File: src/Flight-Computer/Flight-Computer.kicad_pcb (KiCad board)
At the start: 4 copper layers, 113.5 x 45.7 mm, 109 parts, among them J1 Jumper_NO, P1 282837-2, P10 Micro_SD_Card, P2 647676-2, P3 USB, P4 282837-6, P5 440054-3, P6 440054-3, P7 440054-3, P8 3220-20-0200-00, P9 440054-3, Q1 QS5U17TR, Q2 QS5U17TR, Q3 QS5U17TR, Q4 QS5U17TR, Q5 QS5U17TR, Q6 QS5U17TR, U1 STM32H750VBTx, U10 RFM95W-868S2, U11 BMP390, U2 LMS8117AMP-3.3_NOPB, U3 CP2102-GMR(QFN28), U4 SST25VF040B-50-4I-S2AE-T, U5 TS391IYLT, U6 TS391IYLT, U7 TS391IYLT, U8 MPU-9250, U9 MAX-8C-0-10, Y1 ECS-240-18-33-JGN-TR

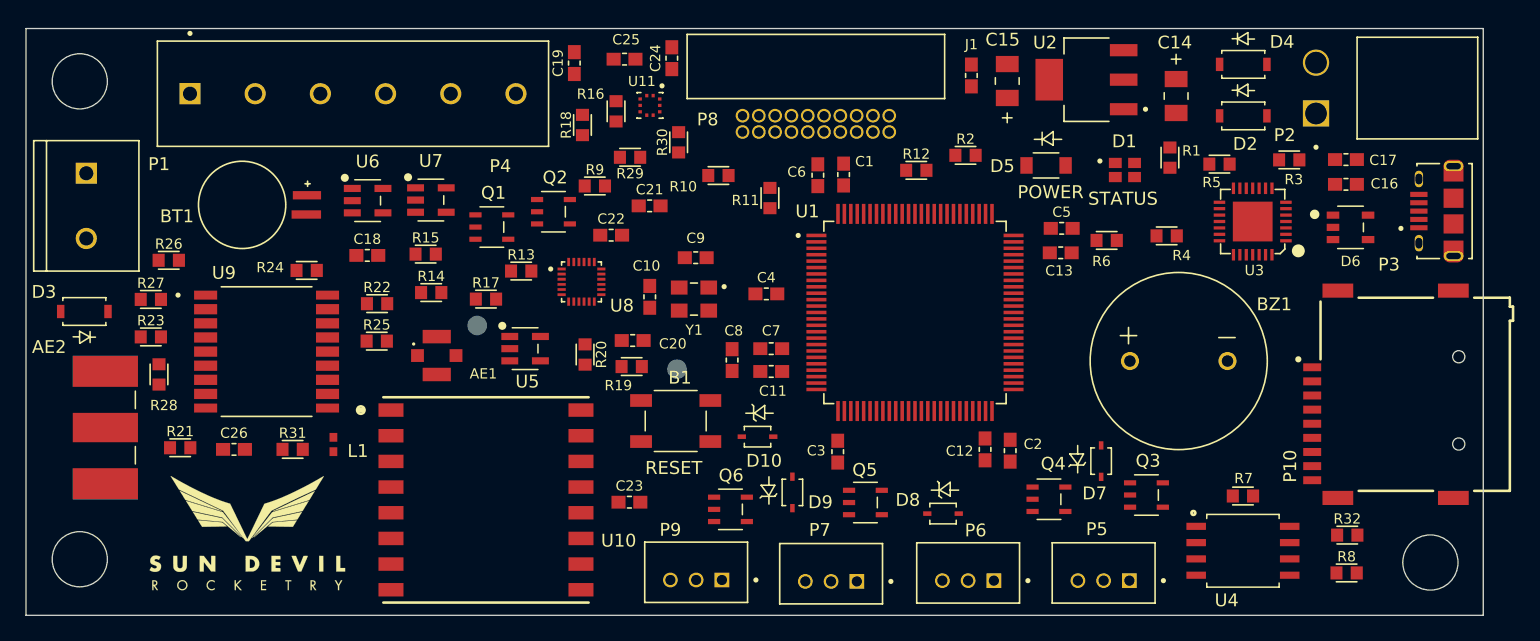
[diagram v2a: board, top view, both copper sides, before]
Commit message: routed main peripheral functionality excluding parachute deployment circuitry
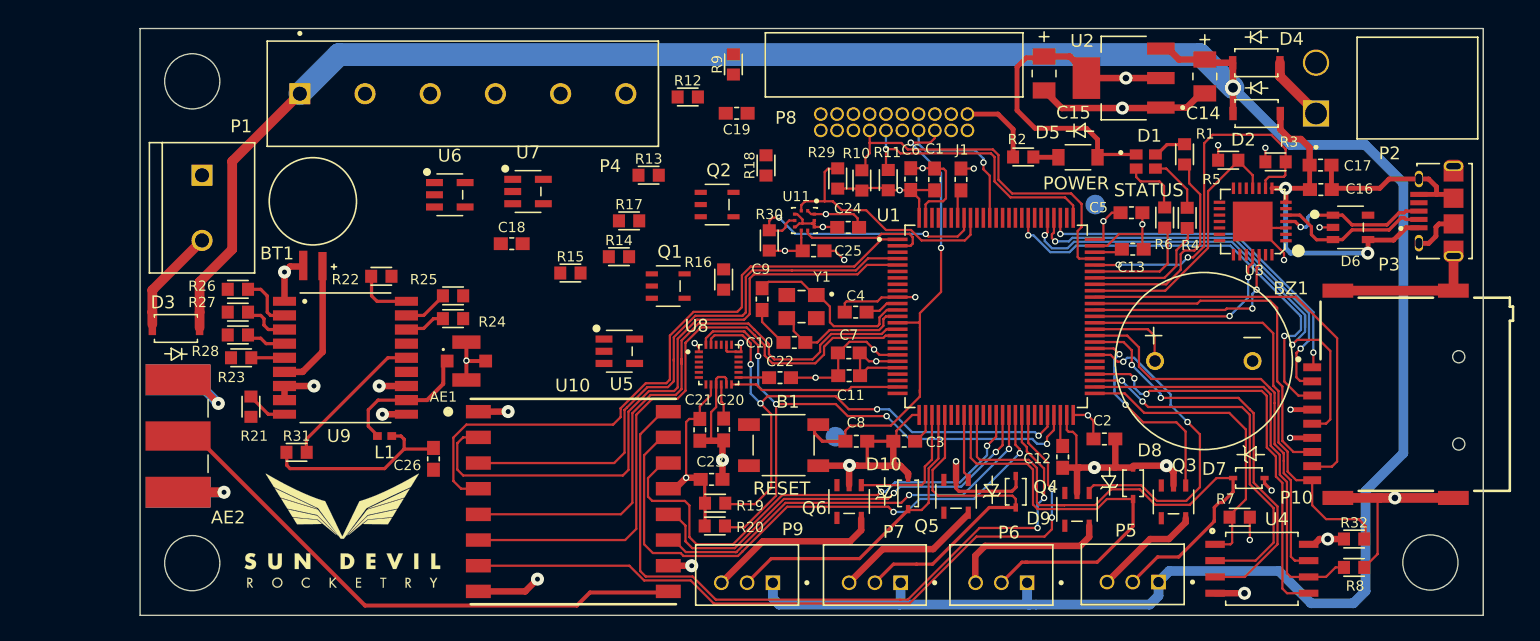
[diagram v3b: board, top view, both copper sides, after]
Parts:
- AE2: value CONN_142-0701-851_CIN -> 142-0701-851
- moved TP2 49.1 mm to (156.5, 69.6)
- moved C25 21.0 mm to (134.5, 73.2)
- moved C24 19.0 mm to (137.2, 71.4), turned to 180 degrees
- moved R12 18.7 mm to (124.7, 61.2)
- moved C21 17.9 mm to (125.7, 87.1), turned to -90 degrees
- moved D9 17.4 mm to (150.3, 92.0)
- moved C22 17.2 mm to (131.9, 83.1)
- moved R20 16.8 mm to (126.8, 94.6), turned to 180 degrees
- moved R29 16.3 mm to (136.4, 67.6), turned to -90 degrees
- moved C26 15.6 mm to (104.9, 89.4), turned to -90 degrees
- moved R16 15.6 mm to (127.5, 75.4)
- moved U11 15.0 mm to (133.9, 70.9)
- moved D8 15.0 mm to (159.4, 91.3), turned to 90 degrees
- moved R14 14.9 mm to (119.4, 73.7)
- moved R18 14.6 mm to (130.8, 66.5)
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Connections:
- U1 pad 17: W_IO0 -> unconnected-(U1-Pad17)
- U1 pad 18: W_IO1 -> unconnected-(U1-Pad18)
- U1 pad 2: unconnected-(U1-Pad2) -> BP_INT
- U1 pad 24: MOTOR1_PWM -> IMU_INT
- U1 pad 25: MOTOR2_PWM -> unconnected-(U1-Pad25)
- U1 pad 28: MOTOR1_EN -> MOTOR4_EN
- U1 pad 29: MOTOR3_PWM -> MOTOR4_PWM
- U1 pad 30: MOTOR4_PWM -> MOTOR2_PWM
- U1 pad 31: BEEP -> unconnected-(U1-Pad31)
- U1 pad 32: W_IO2 -> unconnected-(U1-Pad32)
- U1 pad 33: W_IO3 -> MOTOR2_EN
- U1 pad 34: unconnected-(U1-Pad34) -> MOTOR3_PWM
- U1 pad 35: unconnected-(U1-Pad35) -> MOTOR1_PWM
- U1 pad 38: unconnected-(U1-Pad38) -> W_IO0
- U1 pad 39: unconnected-(U1-Pad39) -> W_IO4
- U1 pad 40: STATUS_R -> W_IO3
- U1 pad 41: STATUS_G -> W_IO1
- U1 pad 42: STATUS_B -> W_IO2
- U1 pad 43: unconnected-(U1-Pad43) -> W_IO5
- U1 pad 46: BP_SCL -> SCL
- U1 pad 47: BP_SDA -> SDA
- U1 pad 57: ~{USB_RST} -> MOTOR3_EN
- U1 pad 58: ~{USB_SUSPEND} -> MOTOR1_EN
- U1 pad 61: BP_INT -> BEEP
- U1 pad 62: unconnected-(U1-Pad62) -> ~{SD_DETECT}
- U1 pad 63: W_IO4 -> RX_USB
- U1 pad 64: W_IO5 -> TX_USB
- U1 pad 67: MOTOR3_EN -> ~{USB_SUSPEND}
- U1 pad 68: RX_USB -> STATUS_B
- U1 pad 69: TX_USB -> STATUS_G
- U1 pad 70: MOTOR2_EN -> STATUS_R
- U1 pad 71: MOTOR4_EN -> ~{USB_RST}
- U1 pad 84: IMU_INT -> unconnected-(U1-Pad84)
- U1 pad 92: SCL -> BP_SCL
- U1 pad 93: SDA -> BP_SDA
- U1 pad 96: ~{SD_DETECT} -> unconnected-(U1-Pad96)
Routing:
- net Earth: track 0.00 -> 210.9 mm, vias 0 -> 30
- net VIN: track 0.00 -> 208.6 mm, vias 0 -> 1
- net 3.3V: track 0.00 -> 90.4 mm, vias 0 -> 15
- net W_IO5: track 0.00 -> 58.0 mm, vias 0 -> 2
- net W_IO2: track 0.00 -> 57.5 mm, vias 0 -> 2
- net W_MOSI: track 0.00 -> 51.4 mm
- net W_SCK: track 0.00 -> 50.4 mm
- net W_RST: track 0.00 -> 49.8 mm
- net W_SS: track 0.00 -> 48.2 mm
- net SDA: track 0.00 -> 47.4 mm, vias 0 -> 4
- net W_IO1: track 0.00 -> 45.8 mm, vias 0 -> 2
- net SCL: track 0.00 -> 45.1 mm, vias 0 -> 4
- net W_MISO: track 0.00 -> 44.6 mm
- net Net-(AE2-Pad1): track 0.00 -> 44.3 mm
- net MOTOR1_PWM: track 0.00 -> 41.2 mm
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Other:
- board size 113.5 x 45.7 mm -> 104.6 x 45.7 mm

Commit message: finished routing
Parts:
- removed TP1: TP, Flight-Computer:TP
- moved R18 20.1 mm to (112.5, 74.9), turned to 0 degrees
- moved R20 17.0 mm to (123.4, 78.0), turned to -90 degrees
- moved Q1 16.1 mm to (109.5, 67.6), turned to 180 degrees
- moved R19 15.9 mm to (126.5, 77.0)
- moved R12 13.8 mm to (112.8, 68.1), turned to -90 degrees
- moved R9 10.3 mm to (126.7, 68.8)
- moved U5 10.2 mm to (124.5, 72.2), turned to 180 degrees
- moved U6 10.0 mm to (115.6, 72.4), turned to 180 degrees
- moved AE1 9.91 mm to (117.4, 82.2)
- moved R14 9.70 mm to (128.8, 71.4), turned to 90 degrees
- moved R31 9.20 mm to (103.4, 89.9), turned to 180 degrees
- moved C23 8.99 mm to (132.6, 84.3), turned to 90 degrees
- moved R26 8.95 mm to (98.6, 77.2)
- moved R23 8.77 mm to (98.6, 83.1)
- moved U9 8.73 mm to (106.7, 82.8)
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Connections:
- U1 pad 25: unconnected-(U1-Pad25) -> GPS_INT
- U1 pad 3: unconnected-(U1-Pad3) -> ~{MAIN_CONT}
- U1 pad 31: unconnected-(U1-Pad31) -> ~{GPS_RST}
- U1 pad 32: unconnected-(U1-Pad32) -> GPS_TIM
- U1 pad 40: W_IO3 -> W_IO1
- U1 pad 41: W_IO1 -> W_IO3
- U1 pad 55: ~{MAIN_CONT} -> unconnected-(U1-Pad55)
- U1 pad 56: ~{DROGUE_CONT} -> unconnected-(U1-Pad56)
- U1 pad 7: unconnected-(U1-Pad7) -> DROGUE
- U1 pad 77: ~{GPS_RST} -> unconnected-(U1-Pad77)
- U1 pad 8: unconnected-(U1-Pad8) -> ~{DROGUE_CONT}
- U1 pad 81: ~{GPS_SBOOT} -> unconnected-(U1-Pad81)
- U1 pad 82: GPS_INT -> unconnected-(U1-Pad82)
- U1 pad 85: GPS_TIM -> unconnected-(U1-Pad85)
- U1 pad 86: DROGUE -> unconnected-(U1-Pad86)
- U1 pad 87: ~{SWITCH} -> MAIN
- U1 pad 88: MAIN -> ~{SWITCH}
- U1 pad 9: unconnected-(U1-Pad9) -> ~{GPS_SBOOT}
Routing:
- net GPS_TIM: track 0.00 -> 68.1 mm, vias 0 -> 2
- net ~{GPS_RST}: track 0.00 -> 63.1 mm, vias 0 -> 2
- net GPS_INT: track 0.00 -> 59.5 mm, vias 0 -> 2
- net GPS_RX: track 0.00 -> 58.9 mm, vias 0 -> 2
- net GPS_TX: track 0.00 -> 54.4 mm, vias 0 -> 2
- net MAIN: track 0.00 -> 40.5 mm, vias 0 -> 2
- net VIN_SW: track 0.00 -> 40.2 mm
- net ~{DROGUE_CONT}: track 0.00 -> 34.7 mm, vias 0 -> 2
- net ~{GPS_SBOOT}: track 0.00 -> 33.5 mm, vias 0 -> 2
- net DROGUE: track 0.00 -> 32.9 mm, vias 0 -> 2
- net VIN: track 208.6 -> 240.0 mm, vias 1 -> 3
- net ~{SWITCH}: track 0.00 -> 27.7 mm, vias 0 -> 2
- net ~{MAIN_CONT}: track 0.00 -> 25.7 mm, vias 0 -> 2
- net 3.3V: track 90.4 -> 114.2 mm, vias 15 -> 20
- net VCOMP: track 0.00 -> 22.0 mm
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- added copper zone on In2.Cu, net 3.3V
- added copper zone on In1.Cu, net Earth
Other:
- board size 104.6 x 45.7 mm -> 96.8 x 45.7 mm
- board text added: "DROGUE"
- board text added: "MAIN"
- board text added: "SWITCH"

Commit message: finished resolving DRC errors
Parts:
- AE2: value 142-0701-851 -> CONN_142-0701-851_CIN
- D10, D7, D8, D9: value MM3Z3V3B -> SOD-323FL_477AB_ONS
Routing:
- net SD_CLK: track 38.6 -> 37.5 mm
- net 3.3V: track 114.2 -> 113.7 mm
- net Earth: track 231.5 -> 231.3 mm, vias 38 -> 39

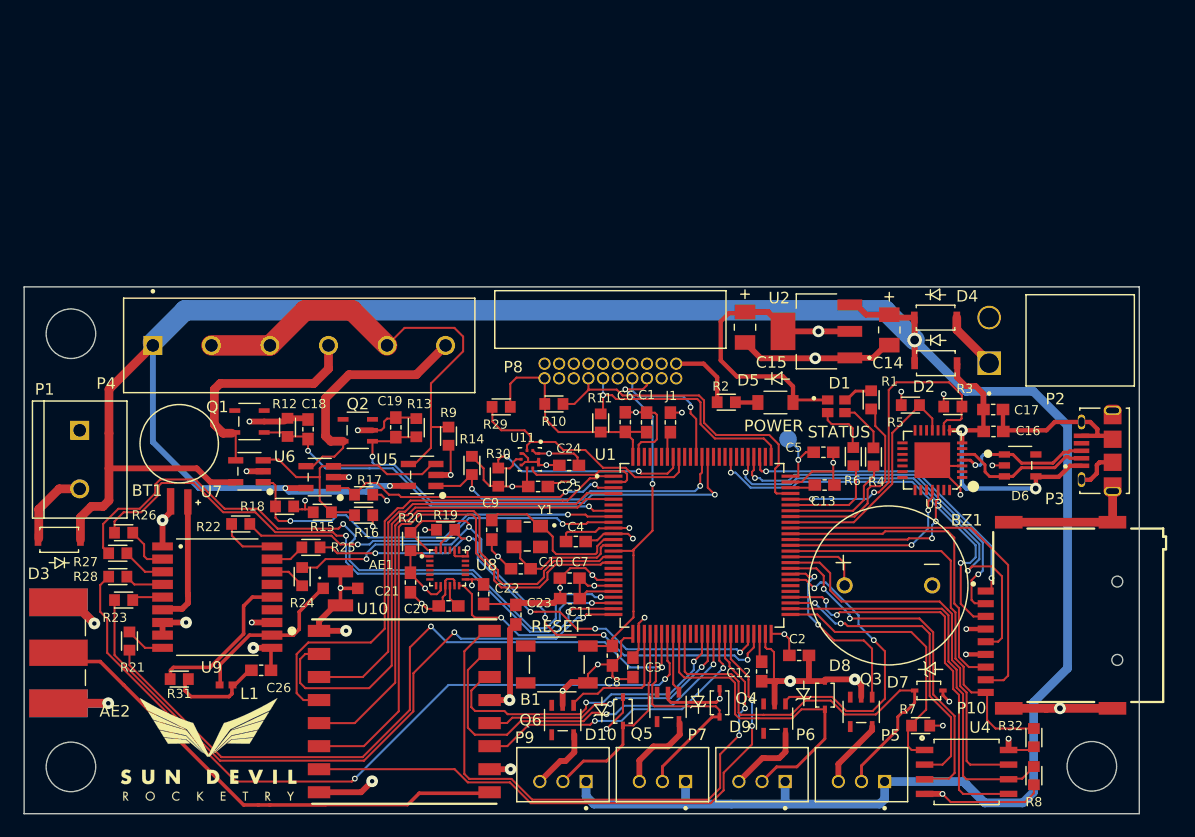
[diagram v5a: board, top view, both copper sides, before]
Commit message: started rev 2 routing
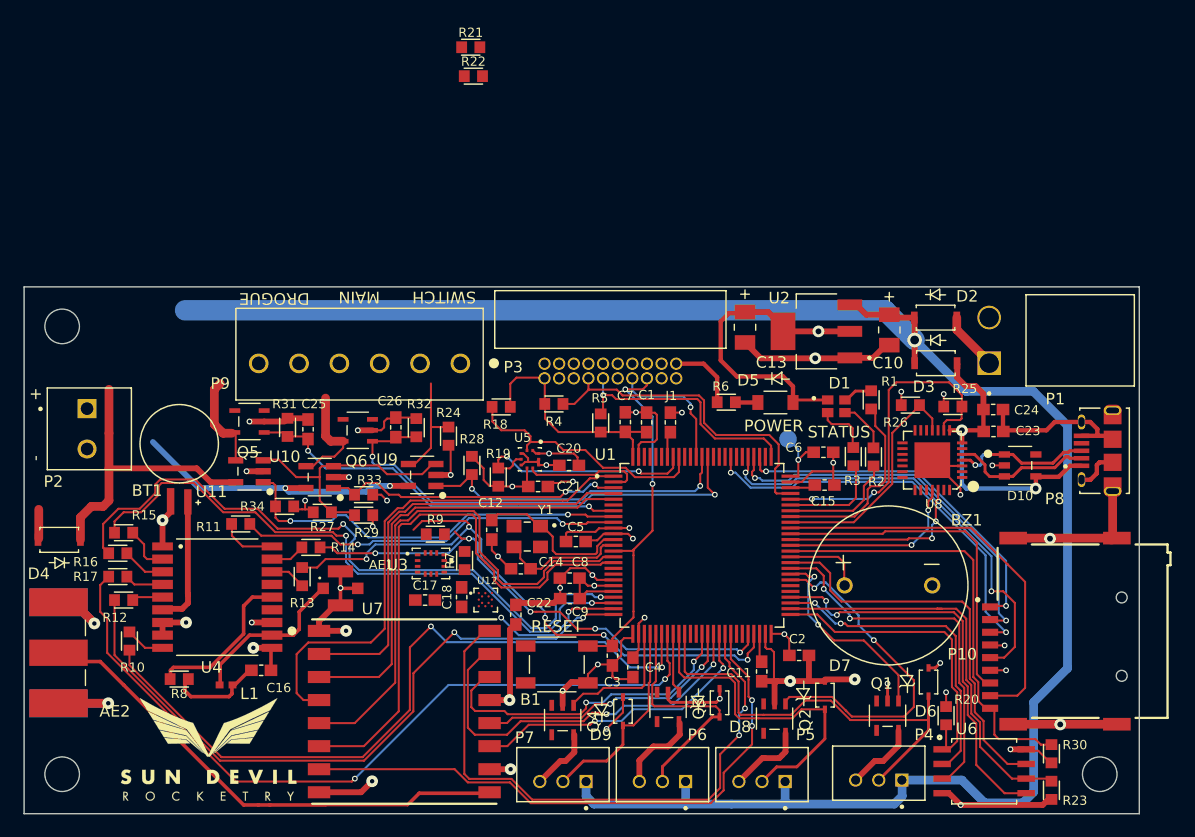
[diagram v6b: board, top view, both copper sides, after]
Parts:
- removed the C20 at (126.7, 83.6)
- removed the C21 at (123.4, 81.5)
- removed the C22 at (129.8, 82.5)
- removed the P1 at (94.7, 70.9)
- removed the P4 at (113.8, 61.0)
- removed the R19 at (126.5, 77.0)
- removed the R20 at (123.4, 78.0)
- removed the U8 at (126.7, 80.3)
- added C17: 0.1uF, Flight-Computer:CAP_0603, F.Cu at (124.7, 83.1)
- added C18: 0.1uF, Flight-Computer:CAP_0603, F.Cu at (127.9, 82.8)
- added P2: 1546551-2, Flight-Computer:1546551-2, F.Cu at (95.4, 68.2)
- added P9: 1984659, Flight-Computer:1984659, F.Cu at (127.8, 62.5)
- added R21: 10k, Flight-Computer:RES_0603, F.Cu at (128.7, 35.1)
- added R22: 20k, Flight-Computer:RES_0603, F.Cu at (128.9, 37.6)
- added R7: 10k, Engine-Controller:RES_0603, F.Cu at (128.1, 79.6)
- added R9: 10k, Engine-Controller:RES_0603, F.Cu at (125.6, 77.3)
- added U12: BMM150, Flight-Computer:BMM150, F.Cu at (130.0, 83.1)
- added U3: BMI323, Flight-Computer:BMI323, F.Cu at (125.2, 79.9)
- AE2: value CONN_142-0701-851_CIN -> 142-0701-851
- D6: renamed from D7; value SOD-323FL_477AB_ONS -> MM3Z3V3B
- D7: renamed from D8; value SOD-323FL_477AB_ONS -> MM3Z3V3B
- D8: renamed from D9; value SOD-323FL_477AB_ONS -> MM3Z3V3B
- D9: renamed from D10; value SOD-323FL_477AB_ONS -> MM3Z3V3B
- H1: footprint Flight-Computer:MountingHole_4.3mm_M4_DIN965 -> Flight-Computer:MountingHole_3mm
- H2: renamed from H3; footprint Flight-Computer:MountingHole_4.3mm_M4_DIN965 -> Flight-Computer:MountingHole_3mm
- H3: renamed from H4; footprint Flight-Computer:MountingHole_4.3mm_M4_DIN965 -> Flight-Computer:MountingHole_3mm
- Q1: renamed from Q3; footprint Engine-Controller:QS5U17TR -> Flight-Computer:QS5U17TR
- Q2: renamed from Q4; footprint Engine-Controller:QS5U17TR -> Flight-Computer:QS5U17TR
- Q3: renamed from Q5; footprint Engine-Controller:QS5U17TR -> Flight-Computer:QS5U17TR
- Q4: renamed from Q6; footprint Engine-Controller:QS5U17TR -> Flight-Computer:QS5U17TR
- Q5: renamed from Q1; footprint Engine-Controller:QS5U17TR -> Flight-Computer:QS5U17TR
- Q6: renamed from Q2; footprint Engine-Controller:QS5U17TR -> Flight-Computer:QS5U17TR
- moved R20 2.37 mm to (169.9, 93.1), turned to 90 degrees
- moved Q1 2.31 mm to (164.8, 93.1)
- moved R30 2.07 mm to (179.1, 96.4)
- moved R23 1.98 mm to (179.1, 99.6)
- moved U6 1.53 mm to (173.2, 97.9)
- moved P4 1.50 mm to (166.1, 98.7)
- moved P10 1.43 mm to (185.2, 86.2)
- moved H1 0.99 mm to (93.2, 59.3)
- moved H2 0.99 mm to (93.2, 98.2)
- moved H3 0.97 mm to (183.3, 98.2)
- moved D6 0.74 mm to (168.4, 90.2), turned to 90 degrees
- renumbered C14 to C10, C12 to C11, C9 to C12, C15 to C13, C10 to C14, C13 to C15, C26 to C16, C24 to C20, C25 to C21, C23 to C22, C16 to C23, C17 to C24, C18 to C25, C19 to C26, C8 to C3, C3 to C4, C4 to C5, C5 to C6, C6 to C7, C7 to C8, C11 to C9, D6 to D10, D4 to D2, D2 to D3, D3 to D4, P2 to P1, P8 to P3, P5 to P4, P6 to P5, P7 to P6, P9 to P7, P3 to P8, R21 to R10, R22 to R11, R23 to R12, R24 to R13, R25 to R14, R26 to R15, R27 to R16, R28 to R17, R29 to R18, R30 to R19, R4 to R2, R7 to R20, R8 to R23, R9 to R24, R3 to R25, R5 to R26, R15 to R27, R14 to R28, R16 to R29, R6 to R3, R32 to R30, R12 to R31, R13 to R32, R17 to R33, R18 to R34, R10 to R4, R11 to R5, R2 to R6, R31 to R8, TP2 to TP1, U6 to U10, U7 to U11, U9 to U4, U11 to U5, U4 to U6, U10 to U7, U3 to U8, U5 to U9
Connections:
- U1 pad 18: unconnected-(U1-Pad18) -> USB_DETECT
- U1 pad 24: IMU_INT -> IMU_INT1
- U1 pad 77: unconnected-(U1-Pad77) -> IMU_INT2
- U1 pad 81: unconnected-(U1-Pad81) -> MAG_INT
- U1 pad 82: unconnected-(U1-Pad82) -> MAG_DRDY
- U7 pad 2: W_MOSI -> W_MISO
- U7 pad 3: W_MISO -> W_MOSI
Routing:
- net VIN_SW: track 40.2 -> 9.66 mm
- net VIN: track 239.7 -> 222.1 mm
- net IMU_INT: track 17.5 -> 0.00 mm, vias 2 -> 0
- net Net-(P9-Pad6): track 20.1 -> 8.14 mm
- net Net-(Q6-Pad5): track 21.3 -> 9.40 mm
- net Earth: track 231.3 -> 219.4 mm
- net IMU_INT1: track 0.00 -> 11.7 mm, vias 0 -> 2
- net 3.3V: track 113.7 -> 103.4 mm, vias 20 -> 17
- net W_MOSI: track 45.0 -> 38.8 mm
- net ~{FLASH_SS}: track 23.0 -> 27.8 mm
- net MOTOR3_EN: track 25.5 -> 29.9 mm
- net /PIN_SCREW: track 6.83 -> 2.54 mm
- net SD_DAT1: track 32.2 -> 35.6 mm
- net SD_DAT3: track 30.9 -> 33.9 mm
- net ~{SD_DETECT}: track 34.6 -> 37.5 mm
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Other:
- board text added: "+"
- board text added: "-"
- board text added: "A0002 Flight Computer Rev 2.0"
- board text removed: "A0002 Flight Computer Rev 1.0"

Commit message: continued rev 2 routing
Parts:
- moved R21 64.1 mm to (178.2, 75.8)
- moved R22 59.4 mm to (174.4, 75.8)
- moved Q4 7.24 mm to (143.9, 93.2)
- moved D9 7.23 mm to (149.1, 92.2)
- moved Q3 6.29 mm to (152.0, 93.2)
- moved D8 5.98 mm to (156.2, 91.3)
- moved C1 5.52 mm to (149.1, 65.7)
- moved R24 5.31 mm to (132.0, 69.8), turned to 180 degrees
- moved R32 4.69 mm to (128.4, 69.6), turned to 180 degrees
- moved Q2 4.47 mm to (159.5, 93.3)
- moved R25 4.18 mm to (174.0, 68.6), turned to 90 degrees
- moved R26 3.82 mm to (170.6, 66.9)
- moved C22 3.77 mm to (134.6, 87.5)
- moved C11 3.66 mm to (157.5, 88.4), turned to 0 degrees
- moved C10 3.63 mm to (165.0, 63.2)
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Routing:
- net 3.3V: track 103.4 -> 74.4 mm, vias 17 -> 18
- net Earth: track 219.4 -> 202.8 mm, vias 39 -> 40
- net MOTOR3_EN: track 29.9 -> 17.7 mm
- net 5V: track 27.5 -> 38.4 mm, vias 2 -> 3
- net MOTOR2_PWM: track 20.9 -> 30.7 mm
- net ~{USB_SUSPEND}: track 20.2 -> 28.3 mm, vias 0 -> 2
- net MOTOR4_PWM: track 17.7 -> 25.1 mm
- net MOTOR2_EN: track 5.27 -> 11.9 mm
- net Net-(P7-Pad3): track 5.57 -> 11.5 mm
- net Net-(Q6-Pad5): track 9.40 -> 3.88 mm
- net MOTOR3_PWM: track 28.8 -> 34.3 mm
- net MOTOR4_EN: track 11.2 -> 6.41 mm
- net W_IO1: track 34.3 -> 29.6 mm
- net BP_SDA: track 20.5 -> 16.5 mm
- net VIN_SW: track 9.66 -> 5.76 mm
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
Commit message: continued rev2 routing
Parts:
- added J2: Jumper_NO, Engine-Controller:Jumper-NO, F.Cu at (137.9, 87.1)
- moved R33 6.14 mm to (125.2, 75.8)
- moved R9 6.02 mm to (128.4, 82.7), turned to -90 degrees
- moved U12 6.00 mm to (135.9, 84.1)
- moved C17 5.47 mm to (130.2, 82.7), turned to 90 degrees
- moved C18 4.95 mm to (132.8, 82.9), turned to 180 degrees
- moved AE1 2.57 mm to (120.0, 82.2)
- moved U3 1.53 mm to (125.9, 81.3), turned to -90 degrees
- moved C22 0.38 mm to (134.2, 87.5)
- moved R7 0.18 mm to (128.3, 79.5)
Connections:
- B1 pad 1: Earth -> Net-(B1-Pad1)
- U1 pad 17: unconnected-(U1-Pad17) -> IMU_INT1
- U1 pad 24: IMU_INT1 -> IMU_INT2
- U1 pad 77: IMU_INT2 -> unconnected-(U1-Pad77)
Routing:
- net IMU_INT2: track 0.00 -> 21.9 mm, vias 0 -> 2
- net IMU_INT1: track 13.5 -> 28.2 mm, vias 1 -> 2
- net 3.3V: track 74.4 -> 88.3 mm, vias 18 -> 22
- net Earth: track 202.8 -> 215.6 mm, vias 40 -> 42
- net Net-(B1-Pad1): track 0.00 -> 7.14 mm, vias 0 -> 1
- net /Navigation and Control/GPS: track 13.9 -> 7.33 mm
- net W_RST: track 47.3 -> 41.2 mm
- net SCL: track 46.8 -> 52.0 mm, vias 5 -> 6
- net VIN: track 219.1 -> 223.7 mm
- net /PIN_HARN: track 4.56 -> 0.00 mm
- net W_SS: track 44.8 -> 40.5 mm
- net ~{GPS_RST}: track 60.2 -> 57.8 mm
- net W_MISO: track 36.0 -> 33.9 mm
- net W_MOSI: track 37.6 -> 35.9 mm
- net ~{MAIN_CONT}: track 26.1 -> 24.6 mm
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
